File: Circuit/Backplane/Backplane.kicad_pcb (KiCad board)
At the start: 2 copper layers, 85.1 x 288.5 mm, 78 parts, among them CON1 peripheral_bridge, CON2 power_distributor, J1 USB_OTG, J2 power_source_mode, J3 general_power_source, J4 pneumatic, J5 pressure_sensor, J6 RS232_DVL, P1 imaging_sonar, P2 DVL, P3 computer1, P4 computer2, P5 ethernet_switch, P6 general, U1 LM1117-3.3, U2 TUSB4041I, U3 TLV73311PDBVT, Y1 24MHz

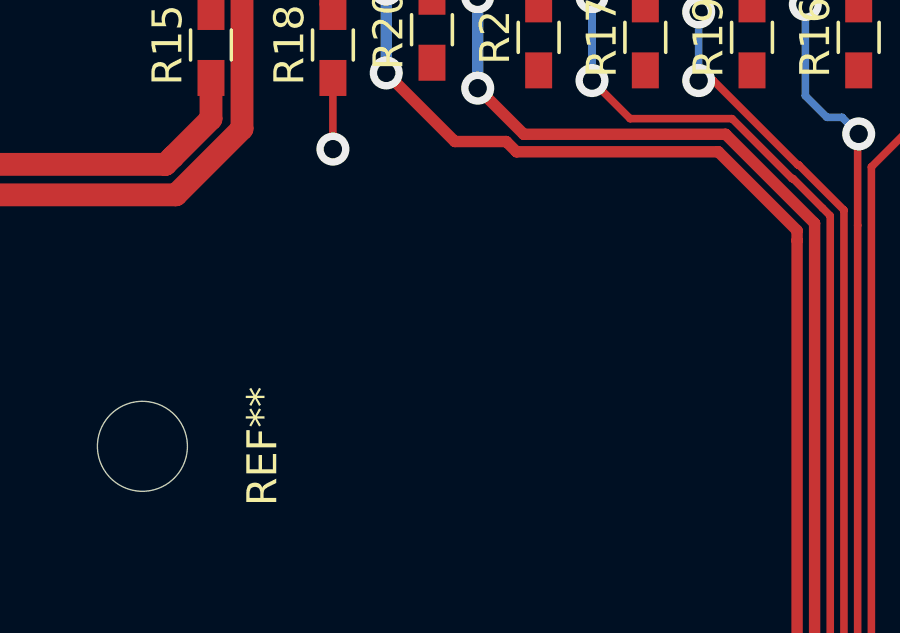
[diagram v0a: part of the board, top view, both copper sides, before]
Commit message: assign NPN's footprint(BC847W -> SOT-323) and generate netlist
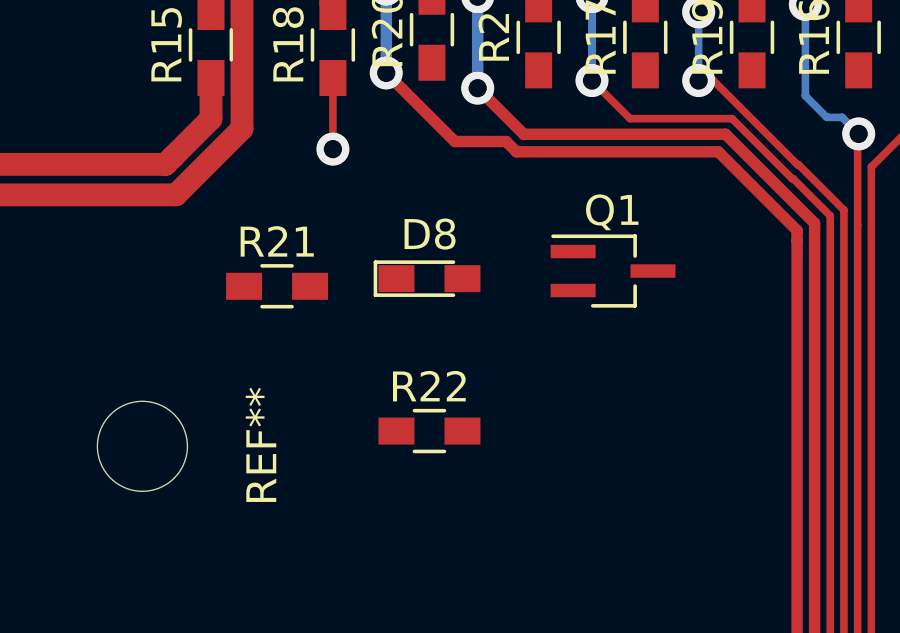
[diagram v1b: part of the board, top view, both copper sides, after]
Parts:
- added D8: LED_1.1V, LEDs:LED_0603_HandSoldering, F.Cu at (150.0, -10.2)
- added Q1: Q_NPN_BCE, TO_SOT_Packages_SMD:SOT-323_SC-70_Handsoldering, F.Cu at (156.2, -10.4)
- added R21: 1k, Resistors_SMD:R_0603_HandSoldering, F.Cu at (144.9, -9.91)
- added R22: 500, Resistors_SMD:R_0603_HandSoldering, F.Cu at (150.0, -5.08)
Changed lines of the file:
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@@
 (kicad_pcb (version 4) (host pcbnew 4.0.7)
   (general
-    (links 251)
-    (no_connects 42)
+    (links 257)
+    (no_connects 49)
     (area 81.204999 -26.745001 166.445001 261.949001)
     (thickness 1.6)
@@
     (tracks 1587)
     (zones 0)
-    (modules 78)
-    (nets 144)
+    (modules 82)
+    (nets 147)
   )
   (page A4)
@@
   )
   (setup
-    (last_trace_width 0.762)
+    (last_trace_width 0.254)
     (user_trace_width 0.381)
     (user_trace_width 0.762)
@@
   (net 142 "Net-(P1-Pad1)")
   (net 143 "Net-(U2-Pad47)")
+  (net 144 "Net-(D8-Pad1)")
+  (net 145 "Net-(Q1-Pad1)")
+  (net 146 "Net-(Q1-Pad2)")
   (net_class Default "This is the default net class."
     (clearance 0.2032)
@@
     (add_net "Net-(D6-Pad1)")
     (add_net "Net-(D7-Pad1)")
+    (add_net "Net-(D8-Pad1)")
     (add_net "Net-(J1-Pad2)")
     (add_net "Net-(J1-Pad3)")
     (add_net "Net-(J1-Pad4)")
     (add_net "Net-(P1-Pad1)")
+    (add_net "Net-(Q1-Pad1)")
+    (add_net "Net-(Q1-Pad2)")
     (add_net "Net-(R1-Pad1)")
     (add_net "Net-(R10-Pad1)")
@@
     (model ${KISYS3DMOD}/Resistors_SMD.3dshapes/R_0603.wrl
       (at (xyz 0 0 0))
+      (scale (xyz 1 1 1))
+      (rotate (xyz 0 0 0))
+    )
+  )
+  (module LEDs:LED_0603_HandSoldering (layer F.Cu)
+    (at 150.03 -10.16)
+    (descr "LED SMD 0603, hand soldering")
+    (tags "LED 0603")
+    (attr smd)
+    (fp_text reference D8 (at 0 -1.45) (layer F.SilkS)
+      (effects (font (size 1 1) (thickness 0.15)))
+    )
+    (fp_text value LED_1.1V (at 0 1.55) (layer F.Fab)
+      (effects (font (size 1 1) (thickness 0.15)))
+    )
+    (fp_line (start -1.8 -0.55) (end -1.8 0.55) (layer F.SilkS) (width 0.12))
+    (fp_line (start -0.2 -0.2) (end -0.2 0.2) (layer F.Fab) (width 0.1))
+    (fp_line (start -0.15 0) (end 0.15 -0.2) (layer F.Fab) (width 0.1))
+    (fp_line (start 0.15 0.2) (end -0.15 0) (layer F.Fab) (width 0.1))
+    (fp_line (start 0.15 -0.2) (end 0.15 0.2) (layer F.Fab) (width 0.1))
+    (fp_line (start 0.8 0.4) (end -0.8 0.4) (layer F.Fab) (width 0.1))
+    (fp_line (start 0.8 -0.4) (end 0.8 0.4) (layer F.Fab) (width 0.1))
+    (fp_line (start -0.8 -0.4) (end 0.8 -0.4) (layer F.Fab) (width 0.1))
+    (fp_line (start -1.8 0.55) (end 0.8 0.55) (layer F.SilkS) (width 0.12))
+    (fp_line (start -1.8 -0.55) (end 0.8 -0.55) (layer F.SilkS) (width 0.12))
+    (fp_line (start -1.96 -0.7) (end 1.95 -0.7) (layer F.CrtYd) (width 0.05))
+    (fp_line (start -1.96 -0.7) (end -1.96 0.7) (layer F.CrtYd) (width 0.05))
+    (fp_line (start 1.95 0.7) (end 1.95 -0.7) (layer F.CrtYd) (width 0.05))
+    (fp_line (start 1.95 0.7) (end -1.96 0.7) (layer F.CrtYd) (width 0.05))
+    (fp_line (start -0.8 -0.4) (end -0.8 0.4) (layer F.Fab) (width 0.1))
+    (pad 1 smd rect (at -1.1 0) (size 1.2 0.9) (layers F.Cu F.Paste F.Mask)
+      (net 144 "Net-(D8-Pad1)"))
+    (pad 2 smd rect (at 1.1 0) (size 1.2 0.9) (layers F.Cu F.Paste F.Mask)
+      (net 3 +5V))
+    (model ${KISYS3DMOD}/LEDs.3dshapes/LED_0603.wrl
+      (at (xyz 0 0 0))
+      (scale (xyz 1 1 1))
+      (rotate (xyz 0 0 180))
+    )
+  )
+  (module TO_SOT_Packages_SMD:SOT-323_SC-70_Handsoldering (layer F.Cu)
+    (at 156.15 -10.414)
+    (descr "SOT-323, SC-70 Handsoldering")
+    (tags "SOT-323 SC-70 Handsoldering")
+    (attr smd)
+    (fp_text reference Q1 (at 0 -2) (layer F.SilkS)
+      (effects (font (size 1 1) (thickness 0.15)))
+    )
+    (fp_text value Q_NPN_BCE (at 0 2.05) (layer F.Fab)
+      (effects (font (size 1 1) (thickness 0.15)))
+    )
+    (fp_text user %R (at 0 0 90) (layer F.Fab)
+      (effects (font (size 0.5 0.5) (thickness 0.075)))
+    )
+    (fp_line (start 0.735 0.5) (end 0.735 1.16) (layer F.SilkS) (width 0.12))
+    (fp_line (start 0.735 -1.17) (end 0.735 -0.5) (layer F.SilkS) (width 0.12))
+    (fp_line (start 2.4 1.3) (end -2.4 1.3) (layer F.CrtYd) (width 0.05))
+    (fp_line (start 2.4 -1.3) (end 2.4 1.3) (layer F.CrtYd) (width 0.05))
+    (fp_line (start -2.4 -1.3) (end 2.4 -1.3) (layer F.CrtYd) (width 0.05))
+    (fp_line (start -2.4 1.3) (end -2.4 -1.3) (layer F.CrtYd) (width 0.05))
+    (fp_line (start 0.735 -1.16) (end -2 -1.16) (layer F.SilkS) (width 0.12))
+    (fp_line (start -0.675 1.16) (end 0.735 1.16) (layer F.SilkS) (width 0.12))
+    (fp_line (start 0.675 -1.1) (end -0.175 -1.1) (layer F.Fab) (width 0.1))
+    (fp_line (start -0.675 -0.6) (end -0.675 1.1) (layer F.Fab) (width 0.1))
+    (fp_line (start 0.675 -1.1) (end 0.675 1.1) (layer F.Fab) (width 0.1))
+    (fp_line (start 0.675 1.1) (end -0.675 1.1) (layer F.Fab) (width 0.1))
+    (fp_line (start -0.175 -1.1) (end -0.675 -0.6) (layer F.Fab) (width 0.1))
+    (pad 1 smd rect (at -1.33 -0.65 270) (size 0.45 1.5) (layers F.Cu F.Paste F.Mask)
+      (net 145 "Net-(Q1-Pad1)"))
+    (pad 2 smd rect (at -1.33 0.65 270) (size 0.45 1.5) (layers F.Cu F.Paste F.Mask)
+      (net 146 "Net-(Q1-Pad2)"))
+    (pad 3 smd rect (at 1.33 0 270) (size 0.45 1.5) (layers F.Cu F.Paste F.Mask)
+      (net 103 GND))
+    (model ${KISYS3DMOD}/TO_SOT_Packages_SMD.3dshapes/SOT-323_SC-70.wrl
+      (at (xyz 0 0 0))
+      (scale (xyz 1 1 1))
+      (rotate (xyz 0 0 0))
+    )
+  )
+  (module Resistors_SMD:R_0603_HandSoldering (layer F.Cu)
+    (at 144.95 -9.906)
+    (descr "Resistor SMD 0603, hand soldering")
+    (tags "resistor 0603")
+    (attr smd)
+    (fp_text reference R21 (at 0 -1.45) (layer F.SilkS)
+      (effects (font (size 1 1) (thickness 0.15)))
+    )
+    (fp_text value 1k (at 0 1.55) (layer F.Fab)
+      (effects (font (size 1 1) (thickness 0.15)))
+    )
+    (fp_text user %R (at 0 0) (layer F.Fab)
+      (effects (font (size 0.4 0.4) (thickness 0.075)))
+    )
+    (fp_line (start -0.8 0.4) (end -0.8 -0.4) (layer F.Fab) (width 0.1))
+    (fp_line (start 0.8 0.4) (end -0.8 0.4) (layer F.Fab) (width 0.1))
+    (fp_line (start 0.8 -0.4) (end 0.8 0.4) (layer F.Fab) (width 0.1))
+    (fp_line (start -0.8 -0.4) (end 0.8 -0.4) (layer F.Fab) (width 0.1))
+    (fp_line (start 0.5 0.68) (end -0.5 0.68) (layer F.SilkS) (width 0.12))
+    (fp_line (start -0.5 -0.68) (end 0.5 -0.68) (layer F.SilkS) (width 0.12))
+    (fp_line (start -1.96 -0.7) (end 1.95 -0.7) (layer F.CrtYd) (width 0.05))
+    (fp_line (start -1.96 -0.7) (end -1.96 0.7) (layer F.CrtYd) (width 0.05))
+    (fp_line (start 1.95 0.7) (end 1.95 -0.7) (layer F.CrtYd) (width 0.05))
+    (fp_line (start 1.95 0.7) (end -1.96 0.7) (layer F.CrtYd) (width 0.05))
+    (pad 1 smd rect (at -1.1 0) (size 1.2 0.9) (layers F.Cu F.Paste F.Mask)
+      (net 146 "Net-(Q1-Pad2)"))
+    (pad 2 smd rect (at 1.1 0) (size 1.2 0.9) (layers F.Cu F.Paste F.Mask)
+      (net 144 "Net-(D8-Pad1)"))
+    (model ${KISYS3DMOD}/Resistors_SMD.3dshapes/R_0603.wrl
+      (at (xyz 0 0 0))
+      (scale (xyz 1 1 1))
+      (rotate (xyz 0 0 0))
+    )
+  )
+  (module Resistors_SMD:R_0603_HandSoldering (layer F.Cu)
+    (at 150.03 -5.08)
+    (descr "Resistor SMD 0603, hand soldering")
+    (tags "resistor 0603")
+    (attr smd)
+    (fp_text reference R22 (at 0 -1.45) (layer F.SilkS)
+      (effects (font (size 1 1) (thickness 0.15)))
+    )
+    (fp_text value 500 (at 0 1.55) (layer F.Fab)
+      (effects (font (size 1 1) (thickness 0.15)))
+    )
+    (fp_text user %R (at 0 0) (layer F.Fab)
+      (effects (font (size 0.4 0.4) (thickness 0.075)))
+    )
+    (fp_line (start -0.8 0.4) (end -0.8 -0.4) (layer F.Fab) (width 0.1))
+    (fp_line (start 0.8 0.4) (end -0.8 0.4) (layer F.Fab) (width 0.1))
+    (fp_line (start 0.8 -0.4) (end 0.8 0.4) (layer F.Fab) (width 0.1))
+    (fp_line (start -0.8 -0.4) (end 0.8 -0.4) (layer F.Fab) (width 0.1))
+    (fp_line (start 0.5 0.68) (end -0.5 0.68) (layer F.SilkS) (width 0.12))
+    (fp_line (start -0.5 -0.68) (end 0.5 -0.68) (layer F.SilkS) (width 0.12))
+    (fp_line (start -1.96 -0.7) (end 1.95 -0.7) (layer F.CrtYd) (width 0.05))
+    (fp_line (start -1.96 -0.7) (end -1.96 0.7) (layer F.CrtYd) (width 0.05))
+    (fp_line (start 1.95 0.7) (end 1.95 -0.7) (layer F.CrtYd) (width 0.05))
+    (fp_line (start 1.95 0.7) (end -1.96 0.7) (layer F.CrtYd) (width 0.05))
+    (pad 1 smd rect (at -1.1 0) (size 1.2 0.9) (layers F.Cu F.Paste F.Mask)
+      (net 145 "Net-(Q1-Pad1)"))
+    (pad 2 smd rect (at 1.1 0) (size 1.2 0.9) (layers F.Cu F.Paste F.Mask)
+      (net 141 +1V1))
+    (model ${KISYS3DMOD}/Resistors_SMD.3dshapes/R_0603.wrl
+      (at (xyz 0 0 0))

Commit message: complete routing with LED 1.1V
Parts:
- moved Q1 29.8 mm to (128.5, -21.5), turned to 180 degrees
- moved R22 21.9 mm to (132.8, -18.5)
- moved R21 19.1 mm to (132.8, -24.6), turned to 180 degrees
- moved D8 17.6 mm to (139.4, -24.2), turned to 270 degrees
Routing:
- net +1V1: track 8.08 -> 273.9 mm, vias 0 -> 12
- net +5V: track 499.6 -> 517.1 mm, vias 18 -> 20
- net GND: track 251.8 -> 263.5 mm, vias 13 -> 15
- net Net-(D8-Pad1): track 0.00 -> 8.56 mm
- net Net-(Q1-Pad2): track 0.00 -> 5.49 mm
- net Net-(Q1-Pad1): track 0.00 -> 3.11 mm
- added copper zone on B.Cu, net GND
- added copper zone on F.Cu, net GND

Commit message: extend Backplane width from 84.836 to 90.170 and relocate locking hole
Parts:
- moved REF** 15.8 mm to (81.4, 122.5)
- moved REF** 12.3 mm to (97.9, 257.3)
- moved REF** 4.16 mm to (144.6, -4.62)
- moved REF** 4.16 mm to (124.6, 154.0)
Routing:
- net +5V: track 517.1 -> 481.7 mm
- removed copper zone on B.Cu, net GND
- removed copper zone on F.Cu, net GND
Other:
- board size 85.1 x 288.5 mm -> 90.2 x 288.5 mm

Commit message: decrease PowerDistributor's Differential wire
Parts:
- moved C21 31.5 mm to (105.7, 248.9), turned to 180 degrees
- moved C12 6.60 mm to (142.0, 242.2)
- moved C13 6.60 mm to (135.9, 242.2)
- moved C15 6.60 mm to (156.3, 234.8)
- moved C17 6.60 mm to (124.7, 219.1)
- moved C2 6.60 mm to (135.5, 254.9)
- moved C4 6.60 mm to (154.2, 242.5)
- moved C9 6.60 mm to (103.7, 230.1)
- moved L4 6.60 mm to (138.9, 242.2)
- moved R1 6.60 mm to (140.6, 254.9)
- moved R10 6.60 mm to (128.0, 253.6)
- moved R4 6.60 mm to (107.4, 240.9)
- moved R6 6.60 mm to (137.8, 259.6)
- moved C10 6.60 mm to (116.1, 248.9)
- moved C14 6.60 mm to (113.8, 219.1)
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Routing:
- net +5V: track 481.7 -> 0.00 mm, vias 20 -> 0
- net +12V: track 379.5 -> 0.00 mm, vias 14 -> 0
- net +3V3: track 352.0 -> 0.00 mm, vias 19 -> 0
- net VBUS: track 361.6 -> 31.3 mm, vias 14 -> 0
- net +1V1: track 273.9 -> 0.00 mm, vias 12 -> 0
- net VPCIE: track 264.3 -> 0.00 mm, vias 14 -> 0
- net GND: track 263.5 -> 0.00 mm, vias 15 -> 0
- net GNDA: track 240.4 -> 0.00 mm, vias 5 -> 0
- net +BATT: track 194.8 -> 0.00 mm, vias 6 -> 0
- net genPow: track 153.4 -> 0.00 mm, vias 6 -> 0
- net Net-(CON1-PadA7): track 139.0 -> 0.00 mm, vias 2 -> 0
- net Net-(CON1-PadA6): track 134.2 -> 0.00 mm, vias 2 -> 0
- net Net-(CON1-PadA4): track 130.1 -> 0.00 mm, vias 2 -> 0
- net Net-(CON1-PadB6): track 123.2 -> 0.00 mm, vias 4 -> 0
- net Net-(C14-Pad1): track 167.2 -> 45.7 mm, vias 17 -> 5
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
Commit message: routing TUSB4041i
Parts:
- moved C17 2.79 mm to (121.9, 219.1)
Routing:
- net Net-(C11-Pad1): track 70.3 -> 180.9 mm, vias 8 -> 15
- net Net-(C14-Pad1): track 45.7 -> 128.3 mm, vias 5 -> 7
- net Net-(R1-Pad1): track 4.94 -> 79.5 mm, vias 0 -> 2
- net Net-(R8-Pad1): track 0.00 -> 34.4 mm
- net Net-(R3-Pad2): track 0.00 -> 14.7 mm, vias 0 -> 2
- net +5V: track 0.00 -> 14.0 mm
- net +3V3: track 0.00 -> 13.6 mm
- net Net-(R11-Pad2): track 0.00 -> 12.5 mm, vias 0 -> 2
- net Net-(R4-Pad2): track 0.00 -> 12.0 mm, vias 0 -> 2
- net Net-(R14-Pad2): track 0.00 -> 11.1 mm
- net Net-(R13-Pad2): track 0.00 -> 9.80 mm
- net Net-(R12-Pad2): track 0.00 -> 9.04 mm
- net +1V1: track 0.00 -> 7.75 mm
- net Net-(R5-Pad2): track 0.00 -> 7.37 mm, vias 0 -> 2

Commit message: add Backplane holded hole x4
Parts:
- added REF**: BackplaneHold3mm, Mounting_Holes:MountingHole_3mm, F.Cu at (83.8, -1.27)
- added REF**: BackplaneHold3mm, Mounting_Holes:MountingHole_3mm, F.Cu at (158.8, -1.27)
- added REF**: BackplaneHold3mm, Mounting_Holes:MountingHole_3mm, F.Cu at (83.8, 219.7)
- added REF**: BackplaneHold3mm, Mounting_Holes:MountingHole_3mm, F.Cu at (158.8, 219.7)
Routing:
- net +3V3: track 13.6 -> 276.2 mm, vias 0 -> 12
- net +5V: track 14.0 -> 186.8 mm, vias 0 -> 2
- net VBUS: track 31.3 -> 198.1 mm, vias 0 -> 2
- net Net-(CON1-PadA13): track 0.00 -> 112.6 mm
- net Net-(CON1-PadA15): track 0.00 -> 111.2 mm
- net Net-(CON1-PadA17): track 0.00 -> 109.6 mm
- net Net-(CON1-PadA12): track 0.00 -> 108.5 mm
- net Net-(CON1-PadA14): track 0.00 -> 107.1 mm
- net Net-(CON1-PadA16): track 0.00 -> 105.6 mm
- net Net-(CON1-PadA18): track 0.00 -> 102.9 mm

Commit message: Backplane
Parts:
- moved D6 10.7 mm to (150.1, -24.5)
- moved R19 10.7 mm to (150.1, -18.2)
- moved D7 7.11 mm to (157.2, -24.2)
- moved R20 7.11 mm to (157.2, -18.5)
- moved D4 3.30 mm to (160.5, -24.5)
- moved R17 3.30 mm to (160.5, -18.2)
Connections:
- P1 pad 1: Net-(P1-Pad1) -> +BATT
- P2 pad 1: Net-(P1-Pad1) -> +BATT
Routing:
- net +12V: track 0.00 -> 429.2 mm, vias 0 -> 16
- net +5V: track 186.8 -> 516.8 mm, vias 2 -> 8
- net VPCIE: track 0.00 -> 303.1 mm, vias 0 -> 10
- net +1V1: track 7.75 -> 297.6 mm, vias 0 -> 10
- net +BATT: track 0.00 -> 246.4 mm, vias 0 -> 8
- net GNDA: track 0.00 -> 228.8 mm, vias 0 -> 11
- net Net-(CON1-PadA7): track 0.00 -> 178.1 mm, vias 0 -> 2
- net Net-(CON1-PadA6): track 0.00 -> 170.9 mm, vias 0 -> 2
- net Net-(CON1-PadA4): track 0.00 -> 166.8 mm, vias 0 -> 2
- net Net-(CON1-PadB6): track 0.00 -> 153.6 mm
- net genPow: track 0.00 -> 147.5 mm, vias 0 -> 4
- net +3V3: track 276.2 -> 399.1 mm, vias 12 -> 14
- net VBUS: track 198.1 -> 320.8 mm
- net GND: track 0.00 -> 38.5 mm, vias 0 -> 15
- net Net-(C26-Pad1): track 0.00 -> 26.9 mm
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- added copper zone on B.Cu, net GND
- added copper zone on F.Cu, net GND
